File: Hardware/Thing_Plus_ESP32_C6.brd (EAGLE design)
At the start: 22.9 x 58.4 mm, 119 parts, among them J1 THING_PLUS_LOGICAL, J4 QWIIC_RIGHT_ANGLE, J5 MICRO-SDFRICTION, Q1 20V/4.2A/52mΩ/1.4W, Q2 20V/4.2A/52mΩ/1.4W, U1 ESP32-C6-WROOM-1-NARROW, U2 RT9080-33GJ5, U3 MCP73831, U4 MAX17048

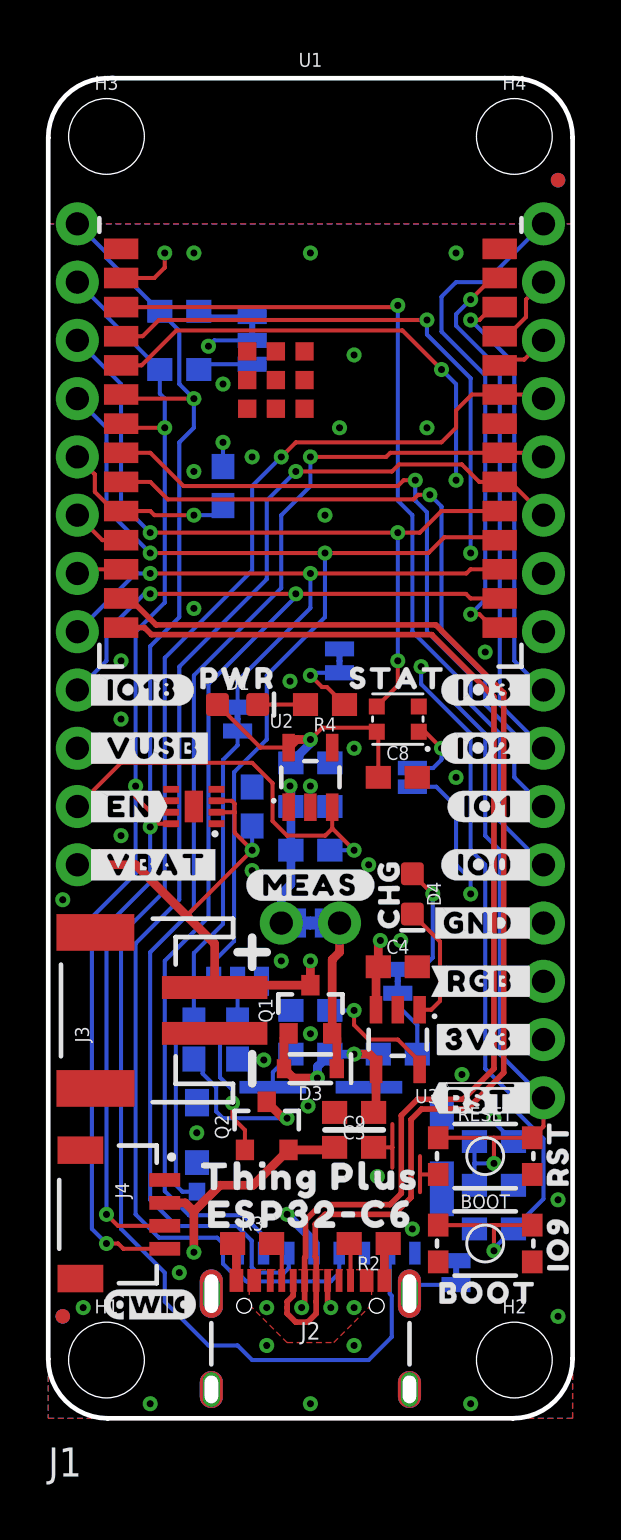
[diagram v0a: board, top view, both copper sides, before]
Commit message: Checklist updates
Add version number to copper
Fix dimension lines to be exactly on grid
Add PROD_ID to ESP32-C6 narrow device
Add layer numbers to copper
Add silk labels to SD_P jumper
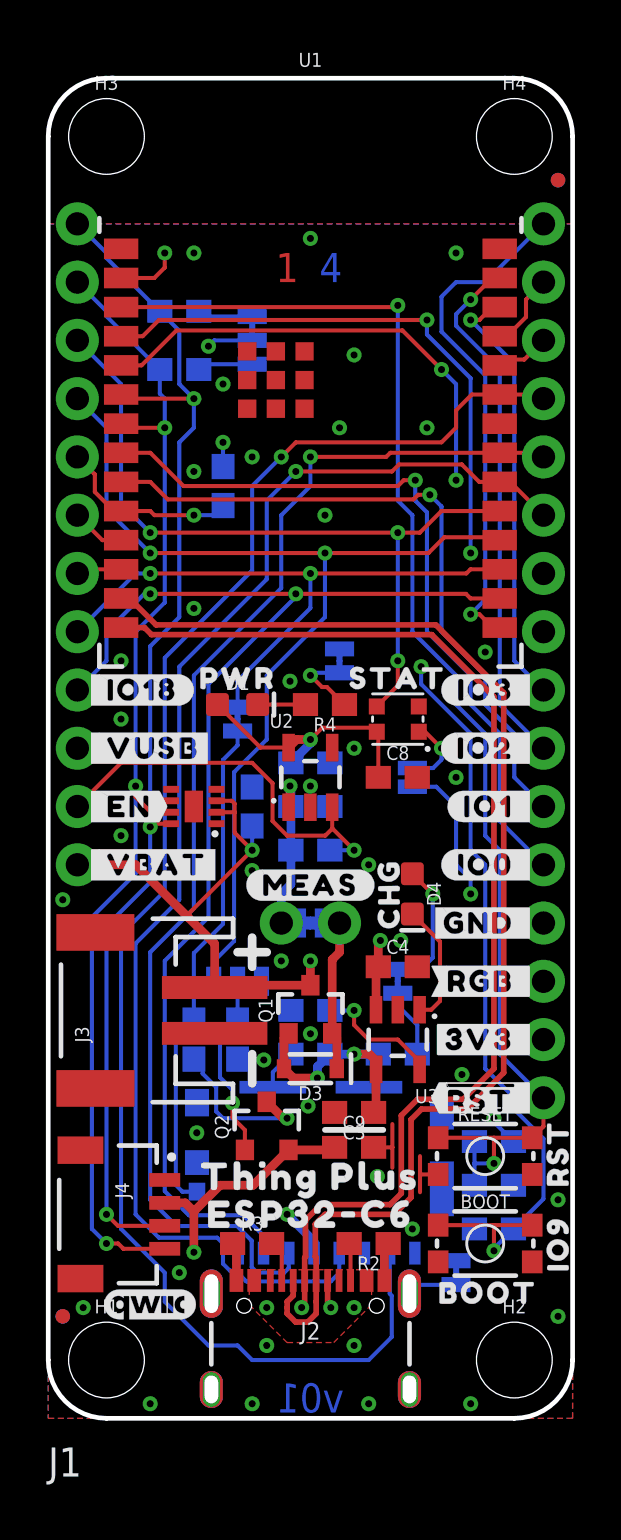
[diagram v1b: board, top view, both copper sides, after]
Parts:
- added U$61: (no value), output:#IO20#0
- added U$63: (no value), output:#G#0
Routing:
- net GND: vias 39 -> 40
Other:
- outline, holes or cut-outs redrawn
- board text added: "1"
- board text added: "2"
- board text added: "3"
- board text added: "4"
- board text added: "v01"
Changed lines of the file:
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@@
 <board>
 <plain>
-<wire x1="0" y1="55.818365625" x2="0" y2="2.58655625" width="0.2032" layer="20"/>
-<wire x1="0" y1="2.58655625" x2="2.58655625" y2="0" width="0.2032" layer="20" curve="90"/>
-<wire x1="2.58655625" y1="0" x2="20.258365625" y2="0" width="0.2032" layer="20"/>
-<wire x1="20.258365625" y1="0" x2="22.86" y2="2.601634375" width="0.2032" layer="20" curve="90"/>
-<wire x1="22.86" y1="2.601634375" x2="22.86" y2="55.83344375" width="0.2032" layer="20"/>
-<wire x1="22.86" y1="55.83344375" x2="20.27344375" y2="58.42" width="0.2032" layer="20" curve="90"/>
-<wire x1="20.27344375" y1="58.42" x2="2.601634375" y2="58.42" width="0.2032" layer="20"/>
-<wire x1="2.601634375" y1="58.42" x2="0" y2="55.818365625" width="0.2032" layer="20" curve="90"/>
 <wire x1="8.89" y1="20.955" x2="8.89" y2="19.685" width="0.381" layer="21"/>
 <wire x1="8.255" y1="20.32" x2="9.525" y2="20.32" width="0.381" layer="21"/>
@@
 <dimension x1="22.86" y1="0" x2="22.86" y2="2.54" x3="26.67" y3="1.27" textsize="1.778" textratio="15" layer="47" unit="inch"/>
 <dimension x1="22.86" y1="0" x2="22.86" y2="13.97" x3="30.48" y3="6.985" textsize="1.778" textratio="15" layer="47" unit="inch"/>
-<dimension x1="0" y1="0" x2="0" y2="58.42" x3="-16.51" y3="29.21" textsize="1.778" textratio="15" layer="47" unit="inch"/>
+<dimension x1="0" y1="0" x2="0" y2="58.42" x3="-20.32" y3="29.21" textsize="1.778" textratio="15" layer="47" unit="inch"/>
 <text x="-16.51" y="-2.54" size="1.778" layer="47" font="vector" ratio="15">Units: Inches</text>
 <text x="35.56" y="40.64" size="1.778" layer="51" font="vector" align="top-left">4-layer
@@
 <wire x1="20.701" y1="11.1125" x2="18.161" y2="11.1125" width="0.254" layer="22"/>
 <wire x1="20.701" y1="9.2075" x2="18.161" y2="9.2075" width="0.254" layer="22"/>
+<text x="11.43" y="0.889" size="1.27" layer="16" font="vector" ratio="15" rot="MR0" align="center">v01</text>
+<wire x1="0" y1="2.54" x2="0" y2="55.88" width="0.2032" layer="20"/>
+<wire x1="2.54" y1="58.42" x2="20.32" y2="58.42" width="0.2032" layer="20"/>
+<wire x1="22.86" y1="55.88" x2="22.86" y2="2.54" width="0.2032" layer="20"/>
+<wire x1="20.32" y1="0" x2="2.54" y2="0" width="0.2032" layer="20"/>
+<wire x1="2.54" y1="0" x2="0" y2="2.54" width="0.2032" layer="20" curve="-90"/>
+<wire x1="0" y1="55.88" x2="2.54" y2="58.42" width="0.2032" layer="20" curve="-90"/>
+<wire x1="20.32" y1="58.42" x2="22.86" y2="55.88" width="0.2032" layer="20" curve="-90"/>
+<wire x1="22.86" y1="2.54" x2="20.32" y2="0" width="0.2032" layer="20" curve="-90"/>
+<text x="10.414" y="50.165" size="1.27" layer="1" font="vector" ratio="15" align="center">1</text>
+<text x="11.049" y="50.165" size="1.27" layer="2" font="vector" ratio="15" align="center">2</text>
+<text x="11.684" y="50.165" size="1.27" layer="15" font="vector" ratio="15" align="center">3</text>
+<text x="12.319" y="50.165" size="1.27" layer="16" font="vector" ratio="15" align="center">4</text>
+<dimension x1="0" y1="0" x2="0" y2="55.88" x3="-16.51" y3="27.94" textsize="1.778" textratio="15" layer="47" unit="inch"/>
 </plain>
 <attributes>
@@
 <element name="U1" library="ESP32-C6-WROOM-1" package="ESP32-C6-WROOM-1-NARROW" value="ESP32-C6-WROOM-1-NARROW" x="11.43" y="45.72" smashed="yes">
 <attribute name="NAME" x="11.43" y="59.22" size="0.6096" layer="25" font="vector" ratio="20" align="center"/>
+<attribute name="PROD_ID" value="IC-19032" x="11.43" y="45.72" size="1.778" layer="27" display="off"/>
 <attribute name="VALUE" x="11.43" y="32.22" size="0.6096" layer="27" font="vector" ratio="20" align="center"/>
 </element>
@@
 </element>
 <element name="U$60" library="output" package="#SD_P#0" value="" x="6.858" y="19.05" smashed="yes" rot="MR0"/>
+<element name="U$61" library="output" package="#IO20#0" value="" x="7.62" y="19.812" smashed="yes" rot="MR90"/>
+<element name="U$63" library="output" package="#G#0" value="" x="8.89" y="19.812" smashed="yes" rot="MR90"/>
 </elements>
 <signals>
@@
 <via x="3.175" y="33.02" extent="1-16" drill="0.3048"/>
 <via x="17.78" y="50.8" extent="1-16" drill="0.3048"/>
-<via x="11.43" y="50.8" extent="1-16" drill="0.3048"/>
+<via x="11.43" y="51.435" extent="1-16" drill="0.3048"/>
 <via x="6.35" y="50.8" extent="1-16" drill="0.3048"/>
 <via x="7.62" y="45.085" extent="1-16" drill="0.3048"/>
@@
 <via x="11.43" y="16.764" extent="1-16" drill="0.3048"/>
 <via x="15.367" y="20.828" extent="1-16" drill="0.3048"/>
-<via x="11.43" y="0.635" extent="1-16" drill="0.3048"/>
+<via x="13.97" y="0.635" extent="1-16" drill="0.3048"/>
 <via x="22.225" y="9.525" extent="1-16" drill="0.3048"/>
 <via x="10.541" y="32.131" extent="1-16" drill="0.3048"/>
@@
 <wire x1="9.7914" y1="15.0864" x2="9.7914" y2="14.434" width="0.1778" layer="16"/>
 <via x="13.97" y="24.13" extent="1-16" drill="0.3048"/>
+<via x="8.89" y="0.635" extent="1-16" drill="0.3048"/>
 </signal>
 <signal name="IO7/SCL">

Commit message: v10 updates
Change pinout of GPIO 15-23 (SDIO pins have funky behavior when not configured)
Connect fuel gauge alert pin
Move SD power control to own circuit that creates VOUT net
Change STAT LED to get powered from VOUT
Change RGB jumper to NC
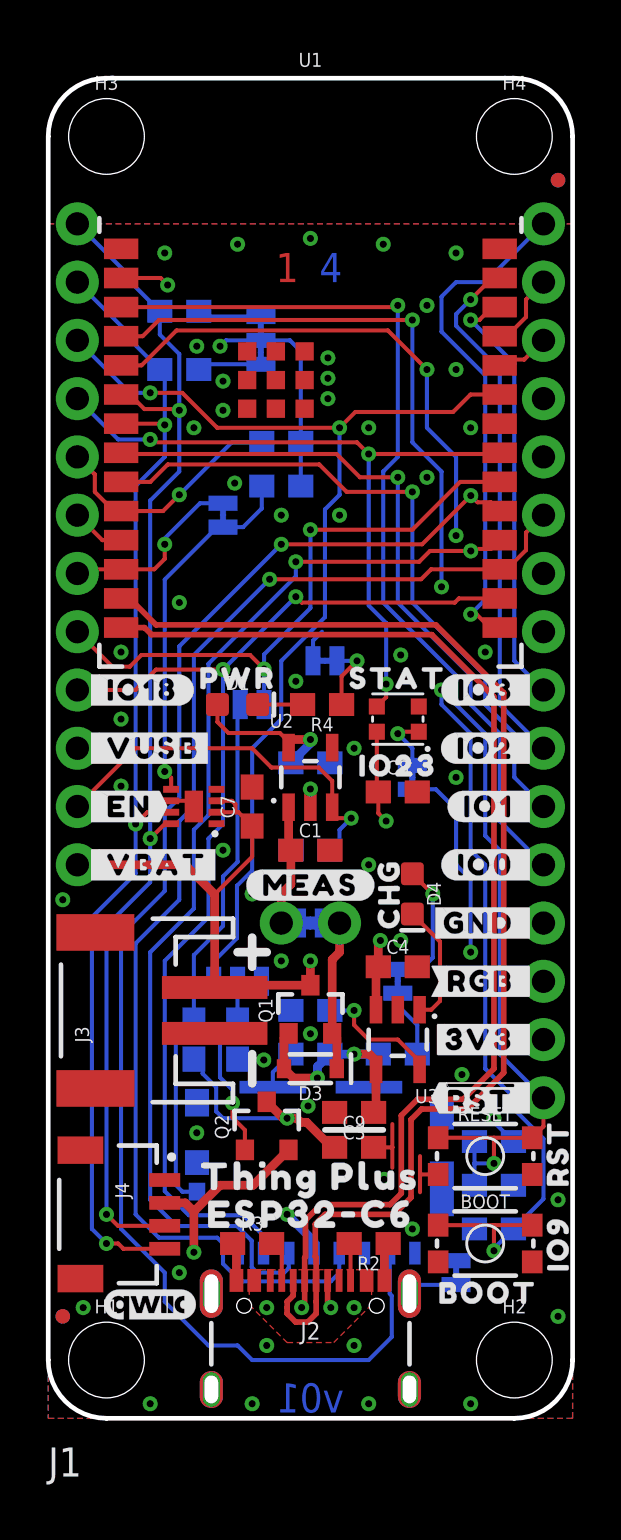
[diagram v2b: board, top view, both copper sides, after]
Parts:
- removed U$60: (no value), output:#SD_P#0
- removed U$61: (no value), output:#IO20#0
- added ALRT: JUMPER-SMT_2_NC_TRACE_SILK, SparkFun-Jumpers:SMT-JUMPER_2_NC_TRACE_SILK
- added R14: 100k, SparkFun-Resistors:0603
- added U$62: (no value), output:IO230
- added U$64: (no value), output:#IO23_#0
- added U$65: (no value), output:#IO15_#0
- added U$66: (no value), output:#IO22_#0
- RGB: value JUMPER-SMT_2_NO_SILK -> JUMPER-SMT_2_NC_TRACE_SILK; device SparkFun-Jumpers:SMT-JUMPER_2_NO_SILK -> SparkFun-Jumpers:SMT-JUMPER_2_NC_TRACE_SILK
- U$16: device output:#IO21_#0 -> output:#_IO21#POCI#0
- U$17: device output:#IO20_#0 -> output:#LP#0
- U$21: device output:#IO19_#0 -> output:#_IO19#SCK#0
- U$26: device output:#_IO15#POCI#0 -> output:#_IO20#PICO#0
- U$27: device output:#_IO23#PICO#0 -> output:#IO15#0
- U$28: device output:#_IO22#SCK#0 -> output:#ALRT#0
- moved U$27 26.0 mm to (7.62, 19.8), turned to 90 degrees
- moved U$17 26.0 mm to (6.86, 19.1)
- moved U$21 20.5 mm to (21.3, 39.4)
- moved U$16 20.0 mm to (21.3, 44.5)
- moved U$28 13.7 mm to (7.62, 40.1), turned to 90 degrees
- moved R1 3.18 mm to (10.2, 42.5), turned to 180 degrees
- moved U$26 2.41 mm to (21.3, 42.0)
- moved C1 1.91 mm to (11.4, 24.8), flipped to the top, turned to 0 degrees
- moved U$41 0.99 mm to (9.65, 31.1)
- moved SD_DET 0.90 mm to (8.89, 31.1), turned to 180 degrees
- moved U$52 0.89 mm to (13.0, 33.0)
- moved C8 0.64 mm to (15.2, 27.3)
- moved PWR 0.63 mm to (12.1, 33.0), turned to 180 degrees
- moved I2C 0.38 mm to (9.27, 47.0)
- moved U$2 0.38 mm to (9.91, 47.0)
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- renumbered SD_P to LP
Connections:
- net IO18/SD_CS renamed IO18/!CS!
- removed net IO11: J1.7, U1.12
- removed net IO15/POCI: J1.16, J5.7, U1.23
- removed net IO19/SD_DET: J1.8, SD_DET.2, U1.17
- removed net IO20/SD_POW: J1.4, LP.1, U1.18
- removed net IO21/STAT: D5.DI, J1.3, U1.19
- removed net IO22/SCK: J1.18, J5.5, U1.20
- removed net IO23/PICO: J1.17, J5.3, U1.21
- removed net N$15: J5.4, Q2.3, R5.2
- new net IO11/!ALRT!: ALRT.2, J1.7, U1.12
- new net IO15/LP: J1.3, LP.1, U1.23
- new net IO19/SCK: J1.18, J5.5, U1.17
- new net IO20/PICO: J1.17, J5.3, U1.18
- new net IO21/POCI: J1.16, J5.7, U1.19
- new net IO22/!SD_DET!: J1.8, SD_DET.2, U1.20
- new net IO23/STAT: D5.DI, J1.4, U1.21
- new net N$17: ALRT.1, R14.1, U4.5
- new net VOUT: C8.1, C9.1, D5.VCC, J5.4, Q2.3, R5.2
- net 3.3V: now also R14.2; no longer C8.1, C9.1, D5.VCC
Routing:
- net IO15/POCI: track 68.6 -> 0.00 mm, vias 1 -> 0
- net IO21/POCI: track 0.00 -> 68.0 mm, vias 0 -> 2
- net IO22/SCK: track 58.7 -> 0.00 mm, vias 1 -> 0
- net IO19/SCK: track 0.00 -> 55.3 mm, vias 0 -> 1
- net IO23/PICO: track 54.4 -> 0.00 mm, vias 1 -> 0
- net IO20/PICO: track 0.00 -> 53.9 mm, vias 0 -> 2
- net IO15/LP: track 0.00 -> 47.0 mm, vias 0 -> 2
- net IO20/SD_POW: track 44.3 -> 0.00 mm, vias 2 -> 0
- net VOUT: track 0.00 -> 37.8 mm, vias 0 -> 3
- net IO21/STAT: track 33.3 -> 0.00 mm, vias 3 -> 0
- net IO23/STAT: track 0.00 -> 30.9 mm, vias 0 -> 3
- net IO22/!SD_DET!: track 0.00 -> 26.8 mm, vias 0 -> 2
- net IO19/SD_DET: track 26.7 -> 0.00 mm, vias 2 -> 0
- net N$17: track 0.00 -> 15.8 mm, vias 0 -> 1
- net N$15: track 13.5 -> 0.00 mm, vias 2 -> 0
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
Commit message: Bump version number to v10
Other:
- board text added: "v10"
- board text removed: "v01"
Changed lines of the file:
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@@
 <wire x1="20.701" y1="11.1125" x2="18.161" y2="11.1125" width="0.254" layer="22"/>
 <wire x1="20.701" y1="9.2075" x2="18.161" y2="9.2075" width="0.254" layer="22"/>
-<text x="11.43" y="0.889" size="1.27" layer="16" font="vector" ratio="15" rot="MR0" align="center">v01</text>
+<text x="11.43" y="0.889" size="1.27" layer="16" font="vector" ratio="15" rot="MR0" align="center">v10</text>
 <wire x1="0" y1="2.54" x2="0" y2="55.88" width="0.2032" layer="20"/>
 <wire x1="2.54" y1="58.42" x2="20.32" y2="58.42" width="0.2032" layer="20"/>
@@
 <element name="FRAME1" library="SparkFun-Aesthetics" package="CREATIVE_COMMONS" value="FRAME-LETTER" x="-11.43" y="-25.4" smashed="yes">
 <attribute name="DESIGNER" value="Dryw Wade" x="-11.43" y="-25.4" size="1.778" layer="27" font="vector" ratio="15" display="off"/>
-<attribute name="REV" value="v01" x="-11.43" y="-25.4" size="1.778" layer="27" font="vector" ratio="15" display="off"/>
+<attribute name="REV" value="v10" x="-11.43" y="-25.4" size="1.778" layer="27" font="vector" ratio="15" display="off"/>
 </element>
 <element name="U1" library="ESP32-C6-WROOM-1" package="ESP32-C6-WROOM-1-NARROW" value="ESP32-C6-WROOM-1-NARROW" x="11.43" y="45.72" smashed="yes">

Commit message: Design review updates
Change schematic frame to ledger
Fix acid trap
Approve DRC errors on jumpers
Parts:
- FRAME1: value FRAME-LETTER -> FRAME-LEDGER
- moved FRAME1 12.6 mm to (-2.54, -34.3)
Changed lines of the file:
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@@
 <drawing>
 <settings>
-<setting alwaysvectorfont="yes"/>
+<setting alwaysvectorfont="no"/>
 <setting verticaltext="up"/>
 </settings>
@@
 </autorouter>
 <elements>
-<element name="FRAME1" library="SparkFun-Aesthetics" package="CREATIVE_COMMONS" value="FRAME-LETTER" x="-11.43" y="-25.4" smashed="yes">
-<attribute name="DESIGNER" value="Dryw Wade" x="-11.43" y="-25.4" size="1.778" layer="27" font="vector" ratio="15" display="off"/>
-<attribute name="REV" value="v10" x="-11.43" y="-25.4" size="1.778" layer="27" font="vector" ratio="15" display="off"/>
-</element>
 <element name="U1" library="ESP32-C6-WROOM-1" package="ESP32-C6-WROOM-1-NARROW" value="ESP32-C6-WROOM-1-NARROW" x="11.43" y="45.72" smashed="yes">
 <attribute name="NAME" x="11.43" y="59.22" size="0.6096" layer="25" font="vector" ratio="20" align="center"/>
@@
 <attribute name="PROD_ID" value="RES-07828" x="10.16" y="40.64" size="1.778" layer="28" rot="MR180" display="off"/>
 <attribute name="VALUE" x="10.16" y="41.402" size="0.6096" layer="28" font="vector" ratio="20" rot="MR180" align="top-center"/>
+</element>
+<element name="FRAME1" library="SparkFun-Aesthetics" package="CREATIVE_COMMONS" value="FRAME-LEDGER" x="-2.54" y="-34.29" smashed="yes">
+<attribute name="DESIGNER" value="Dryw Wade" x="-2.54" y="-34.29" size="1.778" layer="27" display="off"/>
+<attribute name="REV" value="v10" x="-2.54" y="-34.29" size="1.778" layer="27" display="off"/>
 </element>
 </elements>
@@
 <wire x1="7.62" y1="39.8907" x2="6.6167" y2="39.8907" width="0.1778" layer="16"/>
 <via x="5.08" y="38.1" extent="1-16" drill="0.3048"/>
-<wire x1="6.6167" y1="39.8907" x2="5.08" y2="38.354" width="0.1778" layer="16"/>
-<wire x1="5.08" y1="38.354" x2="5.08" y2="38.1" width="0.1778" layer="16"/>
+<wire x1="6.6167" y1="39.8907" x2="5.969" y2="39.243" width="0.1778" layer="16"/>
+<wire x1="5.969" y1="39.243" x2="5.969" y2="38.989" width="0.1778" layer="16"/>
+<wire x1="5.969" y1="38.989" x2="5.08" y2="38.1" width="0.1778" layer="16"/>
 <wire x1="3.18" y1="37.01" x2="4.625" y2="37.01" width="0.1778" layer="1"/>
 <wire x1="5.08" y1="37.465" x2="5.08" y2="38.1" width="0.1778" layer="1"/>
